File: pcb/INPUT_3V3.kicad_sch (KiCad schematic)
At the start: 3 parts

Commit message: updated ethernet
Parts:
- removed C39: 100nF, Capacitor_SMD:C_0603_1608Metric_Pad1.08x0.95mm_HandSolder, symbol Device:C
- removed D9: BZV55C3V6, Diode_SMD:D_MiniMELF, symbol Diode:BZV55C3V6
- removed R27: 100, Resistor_SMD:R_0603_1608Metric_Pad0.98x0.95mm_HandSolder, symbol Device:R
- added C46: 100nF, Capacitor_SMD:C_0603_1608Metric_Pad1.08x0.95mm_HandSolder, symbol Device:C
- added D14: BAT54S, Package_TO_SOT_SMD:SOT-23, symbol Diode:BAT54S
- added R43: 100, Resistor_SMD:R_0603_1608Metric_Pad0.98x0.95mm_HandSolder, symbol Device:R
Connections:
- net IO: now also C46.1, D14.3, R43.2
- net RAW: now also R43.1
- new net 3V3: D14.2 (K)
- new net AGND: C46.2, D14.1 (A)

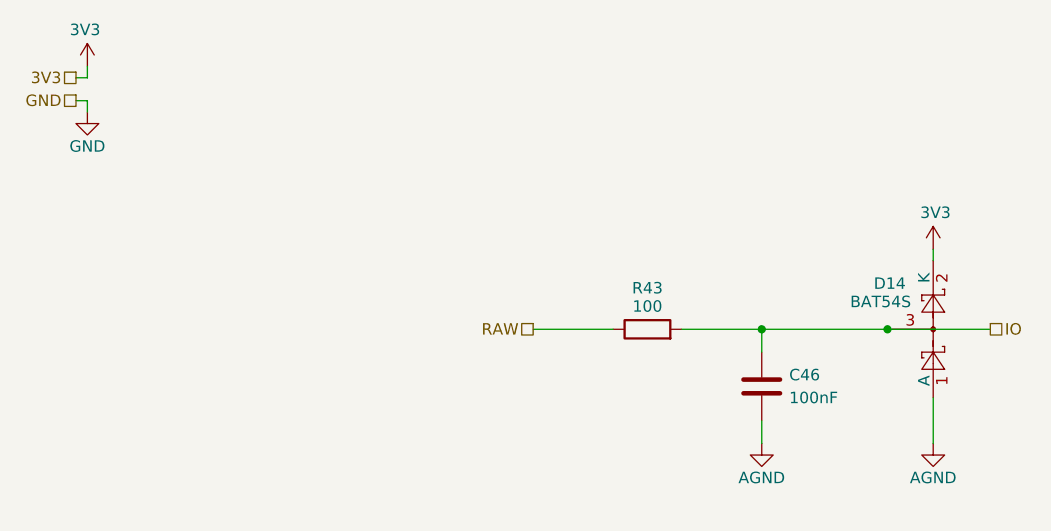
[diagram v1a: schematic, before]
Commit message: reannotated, updated some symbols
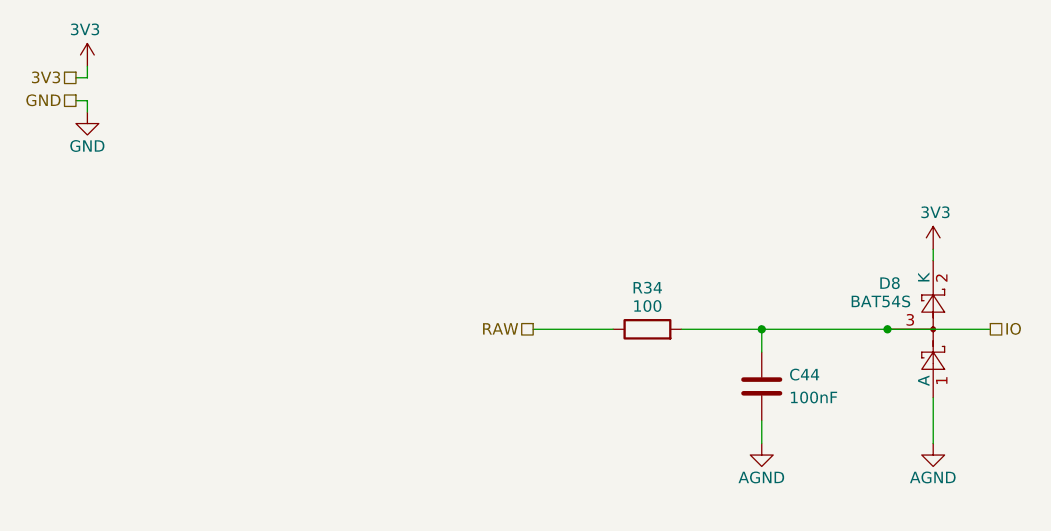
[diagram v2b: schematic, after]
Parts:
- renumbered C46 to C44, D14 to D8, R43 to R34

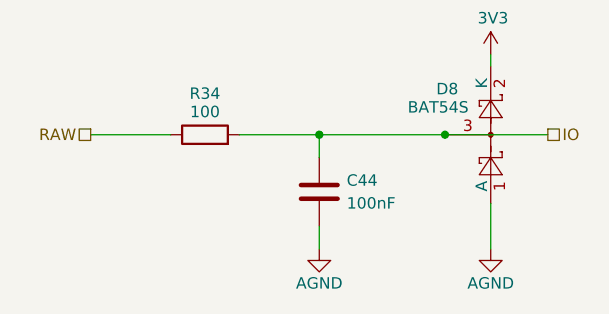
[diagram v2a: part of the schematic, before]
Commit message: removed AGND and added ground garden
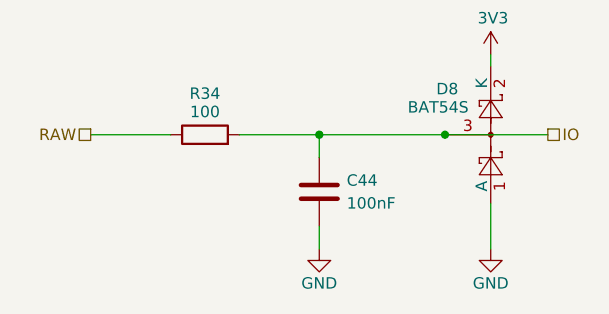
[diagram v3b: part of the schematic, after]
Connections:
- net AGND is gone; now on net GND: C44.2, D8.1 (A)
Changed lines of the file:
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@@
 			)
 		)
-		(property "Value" "AGND"
+		(property "Value" "GND"
 			(at 101.6 67.31 0)
 			(effects
@@
 			)
 		)
-		(property "Value" "AGND"
+		(property "Value" "GND"
 			(at 120.65 67.31 0)
 			(effects

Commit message: updates from bom release
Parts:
- C44: value 100nF -> 100n
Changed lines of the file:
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@@
 			)
 		)
-		(property "Value" "100nF"
+		(property "Value" "100n"
 			(at 104.648 58.42 0)
 			(effects
